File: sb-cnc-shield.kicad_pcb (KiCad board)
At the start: 2 copper layers, 68.6 x 53.3 mm, 63 parts, among them P1 XMOT, P2 YMOT, P3 ZMOT, P4 AMOT, P5 UART, P6 I2C, P7 ES_SETUP, P8 VMOT, SW1 RESET, U1 ARDUINO_UNO_SHIELD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

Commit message: actually properly update shield footprint
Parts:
- JP19: value SE -> SEn
- JP20: value SD -> SDir
- JP21: value COOL -> Cool
- JP22: value ABORT -> Abort
- JP23: value HOLD -> Hold
- P8: value VMOT -> 12V-36V
- U1: footprint footprints:ARDUINO_SHIELD -> sb-cnc-shield:ARDUINO_SHIELD
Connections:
- JP1 pad 1: +5V -> VCC
- JP10 pad 1: +5V -> VCC
- JP11 pad 1: +5V -> VCC
- JP12 pad 1: +5V -> VCC
- JP2 pad 1: +5V -> VCC
- JP3 pad 1: +5V -> VCC
- JP31 pad 1: +5V -> VCC
- JP4 pad 1: +5V -> VCC
- JP5 pad 1: +5V -> VCC
- JP6 pad 1: +5V -> VCC
- JP7 pad 1: +5V -> VCC
- JP8 pad 1: +5V -> VCC
- JP9 pad 1: +5V -> VCC
- P5 pad 2: +5V -> VCC
- P7 pad 1: +5V -> VCC
- R5 pad 1: +5V -> VCC
- U1 pad 16: (no net) -> unconnected-(U1-Pad16)
- U1 pad 17: SCL -> unconnected-(U1-Pad17)
- U1 pad 18: SDA -> unconnected-(U1-Pad18)
- U1 pad 19: COOLANT -> SCL
- U1 pad 20: RESUME -> SDA
- U1 pad 21: HOLD -> COOLANT
- U1 pad 22: ABORT -> RESUME
- U1 pad 23: (no net) -> HOLD
- U1 pad 24: GND -> ABORT
- U1 pad 25: GND -> unconnected-(U1-Pad25)
- U1 pad 26: +5V -> GND
- U1 pad 27: +3V3 -> GND
- U1 pad 28: RESET -> VCC
- U2 pad 10: +5V -> VCC
- U3 pad 10: +5V -> VCC
- U4 pad 10: +5V -> VCC
- U5 pad 10: +5V -> VCC
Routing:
- net VCC: track 0.00 -> 264.8 mm, vias 0 -> 1
- net +5V: track 264.8 -> 0.00 mm, vias 1 -> 0
- net (no net): track 259.9 -> 0.00 mm
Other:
- net class 5V removed
- net class DRV removed
- net class Default removed
- net class POWER removed

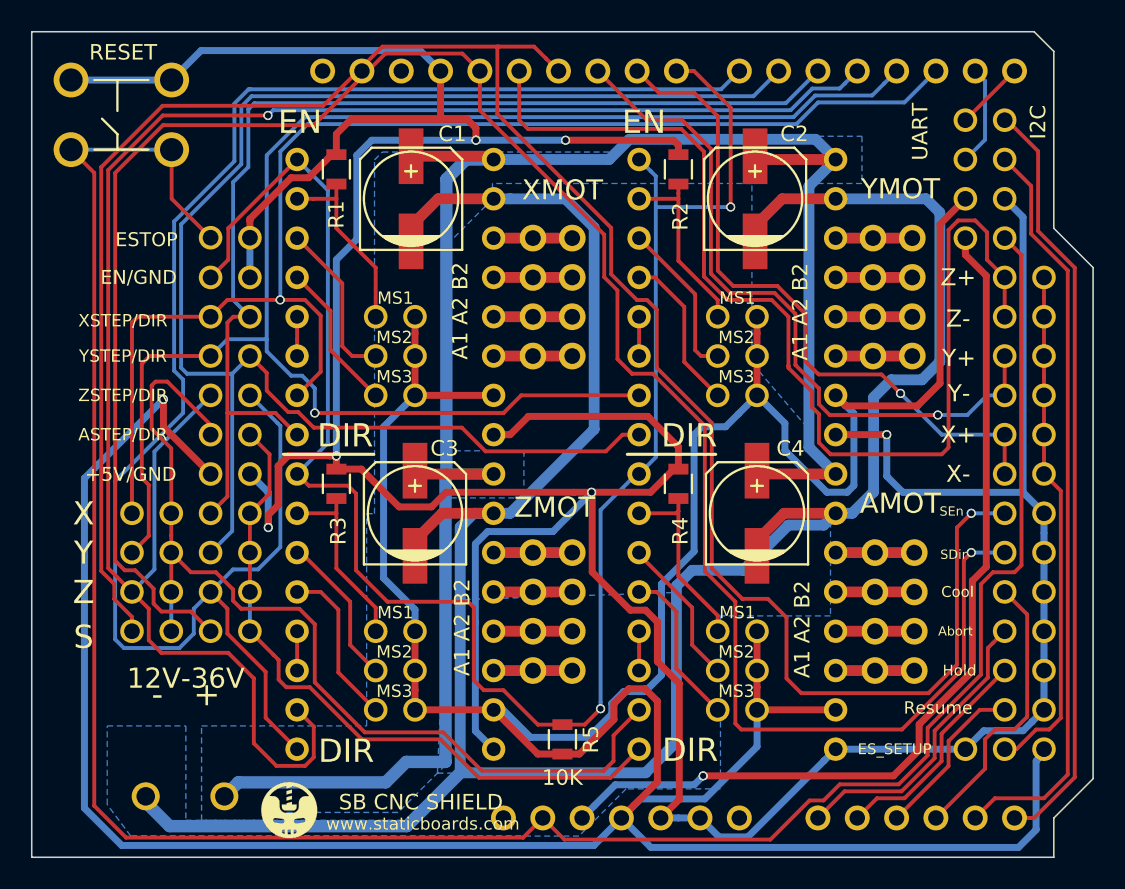
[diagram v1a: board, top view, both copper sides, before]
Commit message: reroute correctly to VCC
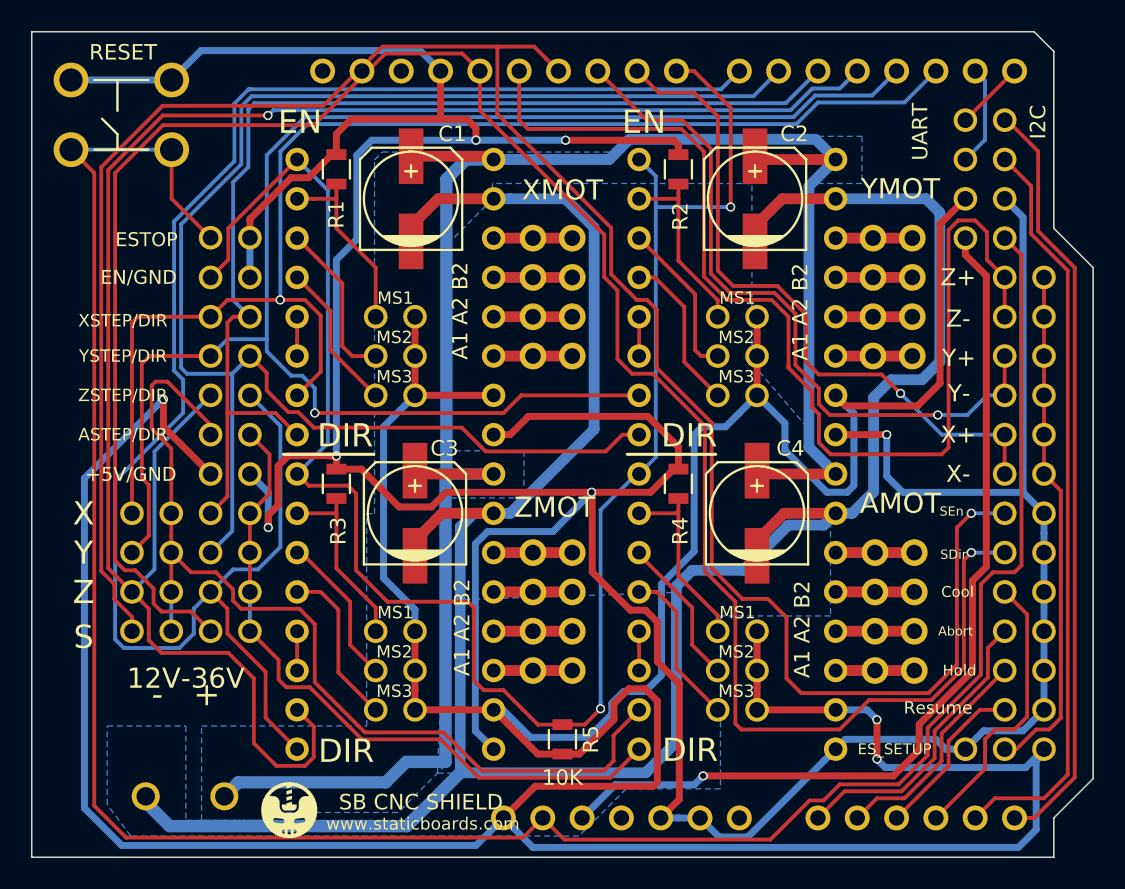
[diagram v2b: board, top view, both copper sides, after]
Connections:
- U1 pad 28: VCC -> +5V
- U1 pad 31: unconnected-(U1-Pad31) -> VCC
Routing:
- net VCC: track 264.8 -> 276.4 mm, vias 1 -> 3
- net GND: track 270.3 -> 270.8 mm

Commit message: make some space for more pins
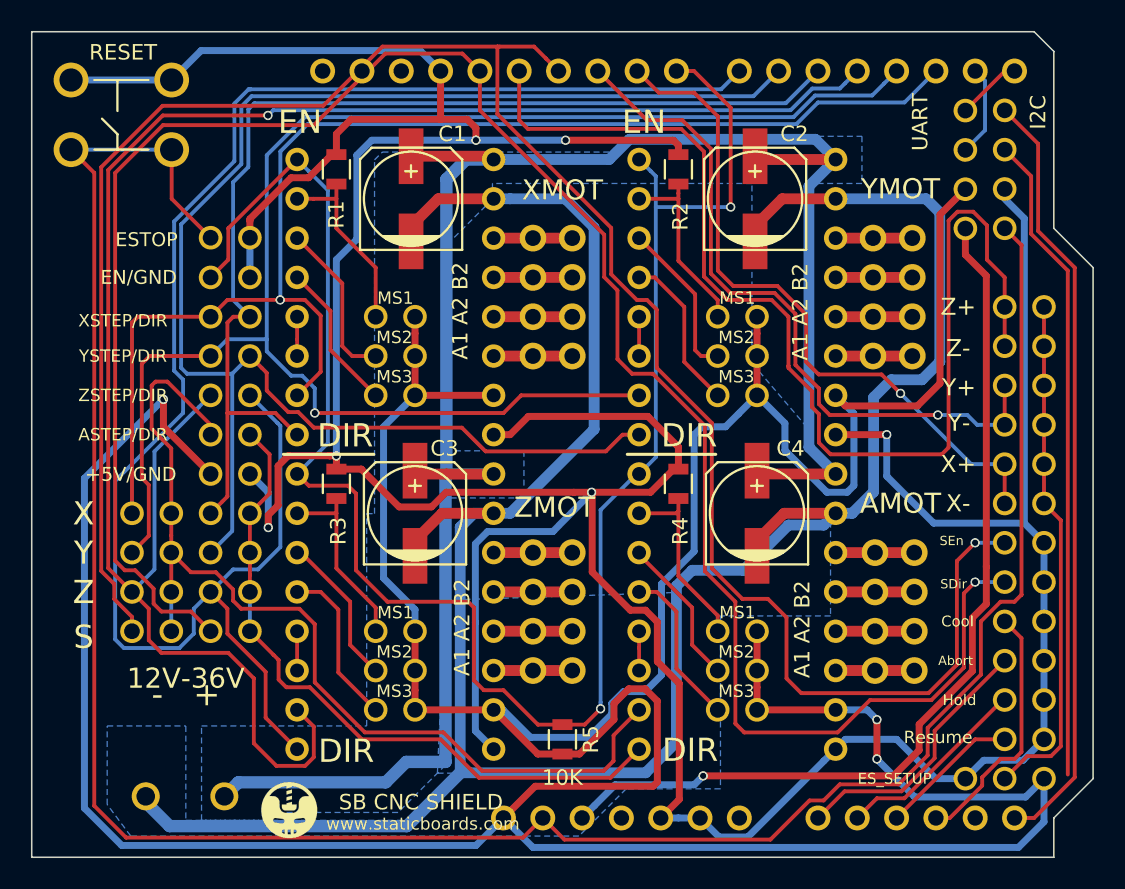
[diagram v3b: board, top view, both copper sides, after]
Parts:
- moved JP14 1.91 mm to (179.7, 86.4)
- moved JP15 1.91 mm to (179.7, 88.9)
- moved JP16 1.91 mm to (179.7, 91.4)
- moved JP17 1.91 mm to (179.7, 94.0)
- moved JP18 1.91 mm to (179.7, 96.5)
- moved JP19 1.91 mm to (179.7, 99.1)
- moved JP20 1.91 mm to (179.7, 101.6)
- moved JP21 1.91 mm to (179.7, 104.1)
- moved JP22 1.91 mm to (179.7, 106.7)
- moved JP23 1.91 mm to (179.7, 109.2)
- moved JP24 1.91 mm to (179.7, 111.8)
- moved P7 1.91 mm to (179.7, 114.3)
- moved JP13 1.90 mm to (179.7, 83.8)
- moved P6 0.64 mm to (177.2, 78.7)
- moved P5 0.62 mm to (174.6, 78.8)
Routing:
- net SDA: track 48.6 -> 42.1 mm
- net GND: track 270.8 -> 274.4 mm
- net ZLIMIT: track 71.4 -> 74.4 mm
- net EN_SETUP: track 33.4 -> 35.9 mm
- net SPIN_EN: track 138.6 -> 136.6 mm
- net ABORT: track 19.2 -> 17.3 mm
- net COOLANT: track 18.4 -> 16.5 mm
- net SPIN_DIR: track 137.4 -> 135.5 mm
- net HOLD: track 14.5 -> 12.7 mm
- net RESUME: track 10.8 -> 9.09 mm
- net XLIMIT: track 43.6 -> 44.4 mm
- net SCL: track 49.4 -> 50.1 mm
- net +3V3: track 59.0 -> 59.7 mm
- net TX: track 6.66 -> 6.04 mm

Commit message: use the real scl/sda pins
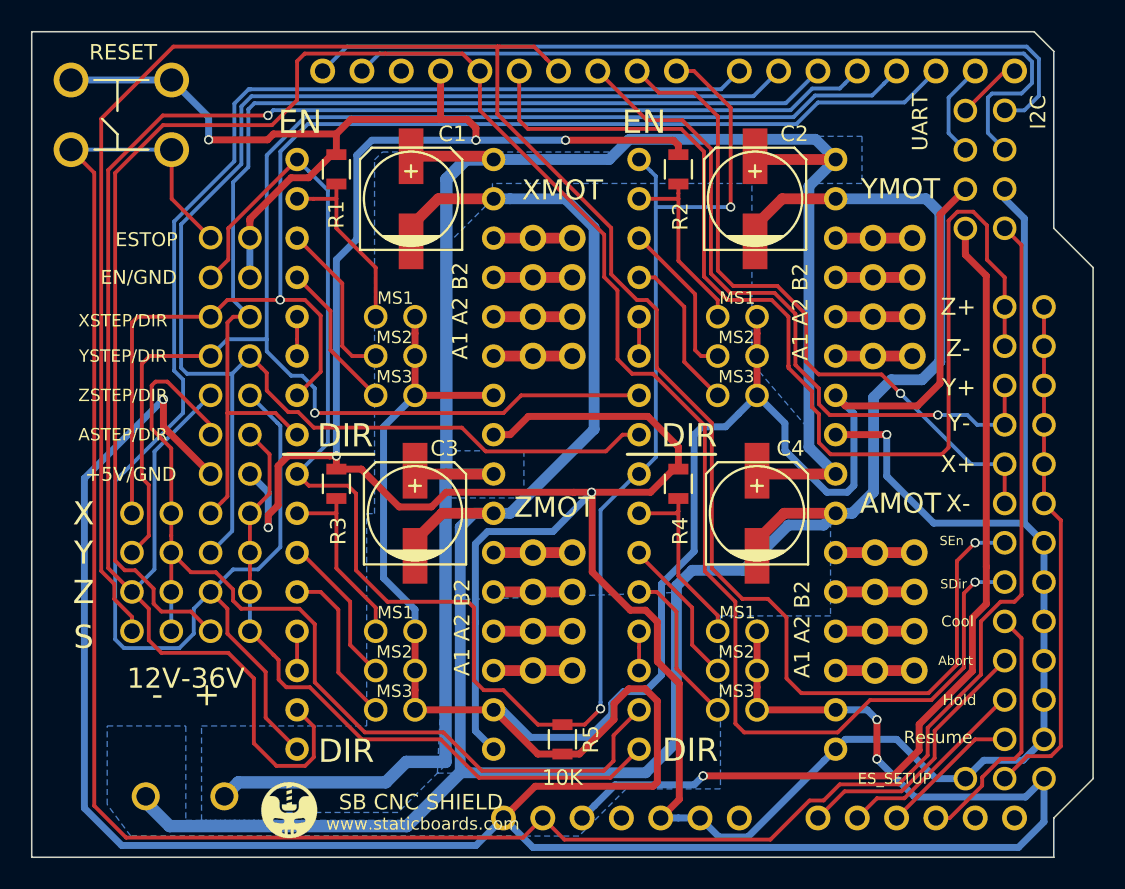
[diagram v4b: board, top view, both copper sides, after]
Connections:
- U1 pad 17: unconnected-(U1-Pad17) -> SDA
- U1 pad 18: unconnected-(U1-Pad18) -> SCL
- U1 pad 19: SCL -> unconnected-(U1-Pad19)
- U1 pad 20: SDA -> unconnected-(U1-Pad20)
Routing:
- net SDA: track 42.1 -> 52.4 mm
- net GND: track 274.4 -> 269.0 mm, vias 6 -> 7
- net SCL: track 50.1 -> 52.4 mm
- net SPIN_EN: track 136.6 -> 138.4 mm
- net SPIN_DIR: track 135.5 -> 137.0 mm

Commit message: more changes
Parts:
- added JP40: Jumper_NO_Small, Jumper:SolderJumper-2_P1.3mm_Open_Pad1.0x1.5mm, F.Cu at (163.8, 113.7)
- added JP41: Jumper_NO_Small, Jumper:SolderJumper-2_P1.3mm_Open_Pad1.0x1.5mm, F.Cu at (161.3, 113.7)
- added R6: 1K, Resistor_SMD:R_0805_2012Metric, F.Cu at (168.9, 111.8)
- added R7: 10K, Resistor_SMD:R_0805_2012Metric, F.Cu at (147.3, 90.2)
- JP31: value +5V/GND -> VCC/GND
- P1: value XMOT -> X
- P2: value YMOT -> Y
- P3: value ZMOT -> Z
- P4: value AMOT -> A
- P5: value UART -> Conn_01x05; footprint Pin_Headers:Pin_Header_Straight_1x04 -> Connector_PinHeader_2.54mm:PinHeader_1x05_P2.54mm_Vertical
- moved P5 2.52 mm to (174.6, 81.3)
- moved G*** 0.33 mm to (130.9, 116.0)
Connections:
- P5 pad 1: +3V3 -> +5V
- P5 pad 2: VCC -> +3V3
- P5 pad 3: TX -> VCC
- P5 pad 4: RX -> TX
- U1 pad 19: unconnected-(U1-Pad19) -> TMC_RX
- U1 pad 20: unconnected-(U1-Pad20) -> TMC_TX
- U2 pad 5: Net-(U2-Pad5) -> TMC_UART
- U2 pad 6: Net-(U2-Pad5) -> TMC_UART
- U3 pad 5: Net-(U3-Pad5) -> TMC_UART
- U3 pad 6: Net-(U3-Pad5) -> TMC_UART
- U4 pad 5: Net-(U4-Pad5) -> TMC_UART
- U4 pad 6: Net-(U4-Pad5) -> TMC_UART
- U5 pad 5: Net-(U5-Pad5) -> TMC_UART
- U5 pad 6: Net-(U5-Pad5) -> TMC_UART
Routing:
- net TMC_UART: track 0.00 -> 101.9 mm, vias 0 -> 6
- net +5V: track 0.00 -> 56.1 mm
- net TMC_RX: track 0.00 -> 19.6 mm
- net TMC_TX: track 0.00 -> 15.1 mm
- net SPIN_DIR: track 137.0 -> 124.6 mm
- net ZLIMIT: track 74.4 -> 62.5 mm, vias 0 -> 1
- net SPIN_EN: track 138.4 -> 127.5 mm
- net GND: track 269.0 -> 258.9 mm
- net Net-(JP40-Pad2): track 0.00 -> 5.60 mm
- net VCC: track 275.9 -> 278.8 mm, vias 3 -> 2
- net RESET: track 151.9 -> 154.7 mm, vias 0 -> 2
- net Net-(U3-Pad5): track 2.54 -> 0.00 mm
- net Net-(U2-Pad5): track 2.54 -> 0.00 mm
- net Net-(U5-Pad5): track 2.54 -> 0.00 mm
- net Net-(U4-Pad5): track 2.54 -> 0.00 mm
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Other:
- board text added: "3V3"
- board text added: "5V"
- board text added: "GND"
- board text added: "RST"
- board text added: "RX"
- board text added: "SCL"
- board text added: "SDA"
- board text added: "TMC Edition"
- board text added: "TMC_UART_EN"
- board text added: "TX"
- board text added: "VCC"
- board text added: "staticboards.com"
- board text removed: "www.staticboards.com"

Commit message: run DRC
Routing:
- net TMC_UART: track 101.9 -> 124.0 mm, vias 6 -> 7
- net GND: track 258.9 -> 269.9 mm
- net +3V3: track 57.9 -> 60.2 mm
- net ZLIMIT: track 62.5 -> 60.6 mm
- net VIN: track 126.7 -> 124.9 mm

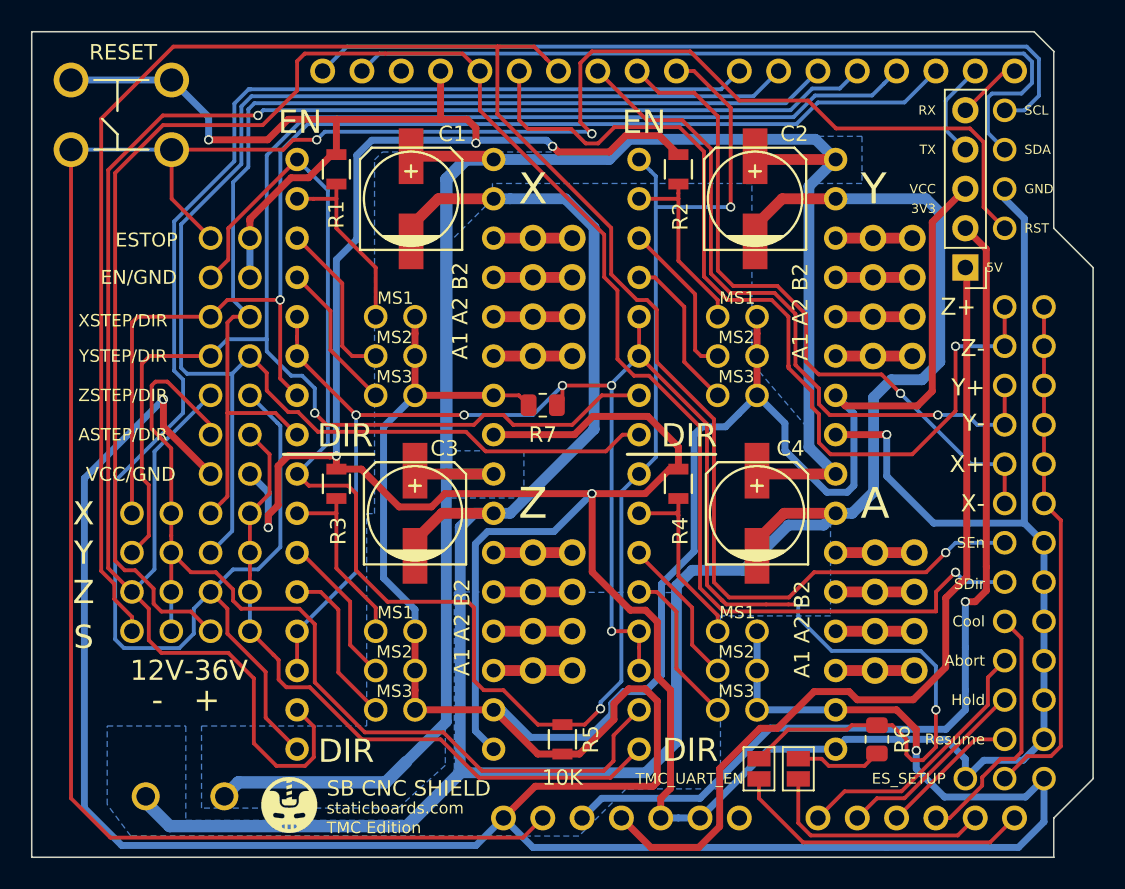
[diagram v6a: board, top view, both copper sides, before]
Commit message: adjust to jlcpcb design rules
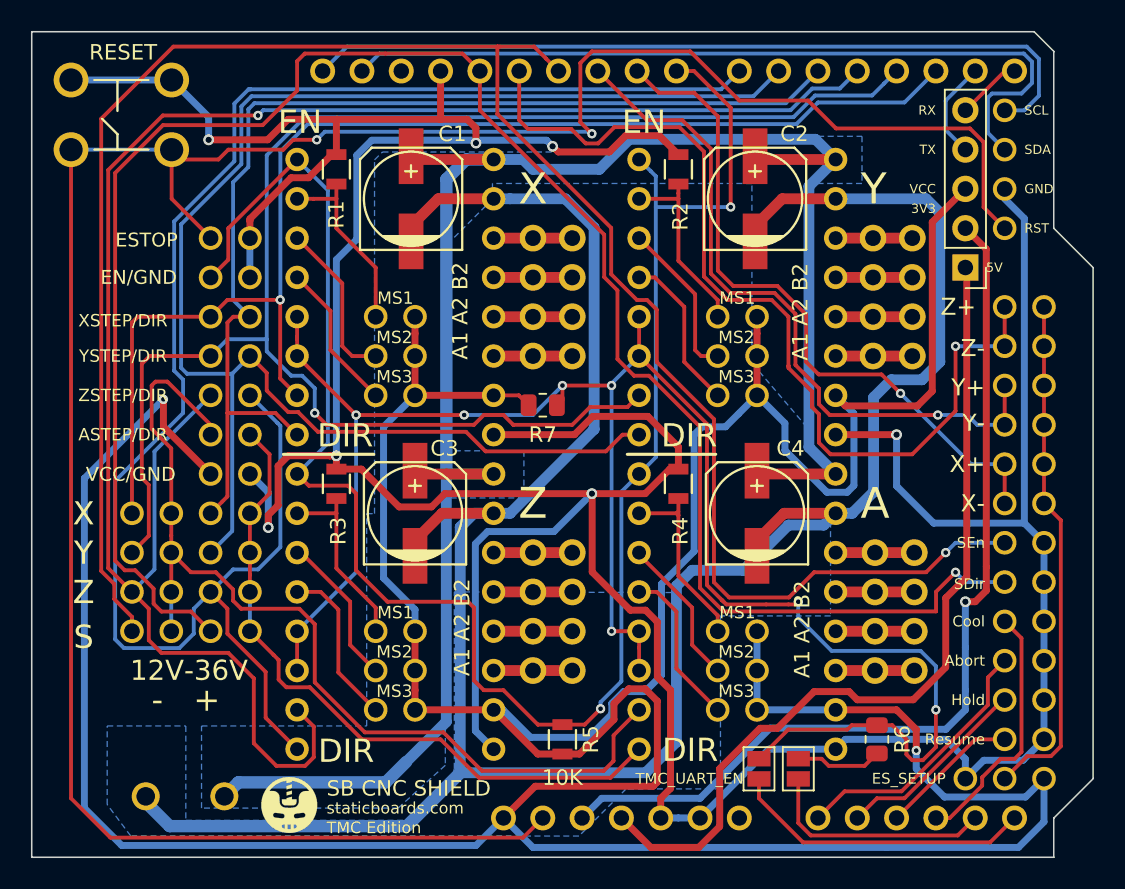
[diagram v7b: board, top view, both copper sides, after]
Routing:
- net VIN: track 124.9 -> 125.4 mm
- net RESET: track 154.7 -> 155.2 mm

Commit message: some more small edits
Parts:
- JP40, JP41: footprint Jumper:SolderJumper-2_P1.3mm_Open_Pad1.0x1.5mm -> Jumper:SolderJumper-2_P1.3mm_Open_TrianglePad1.0x1.5mm
